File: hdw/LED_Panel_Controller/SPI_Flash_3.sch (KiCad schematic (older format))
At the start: 14 parts

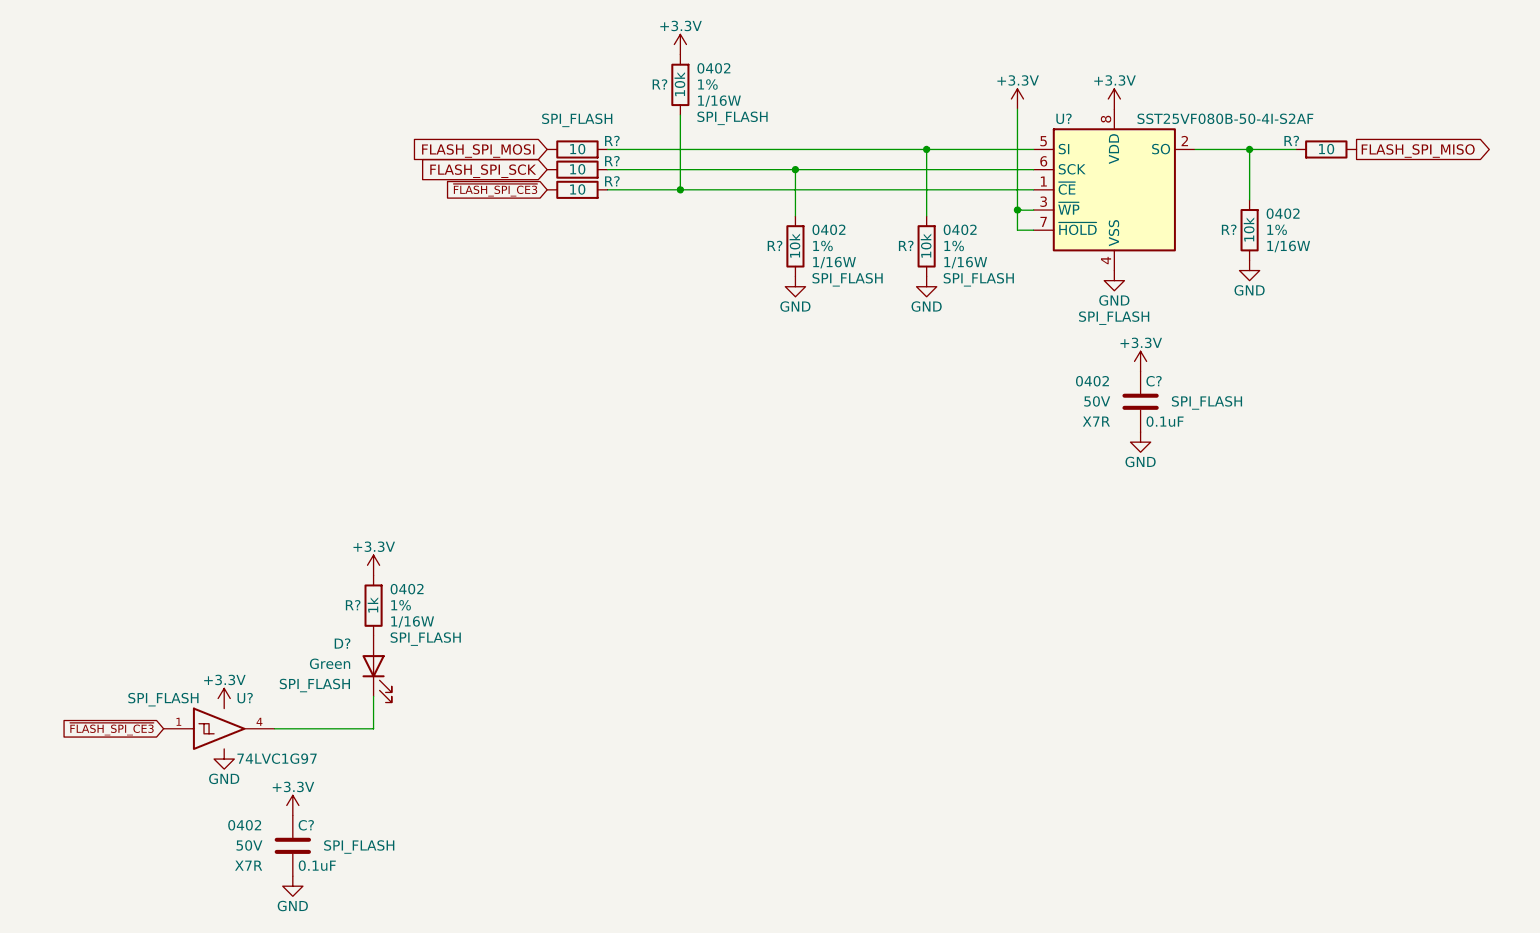
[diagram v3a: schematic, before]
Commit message: assigned I2C addresses
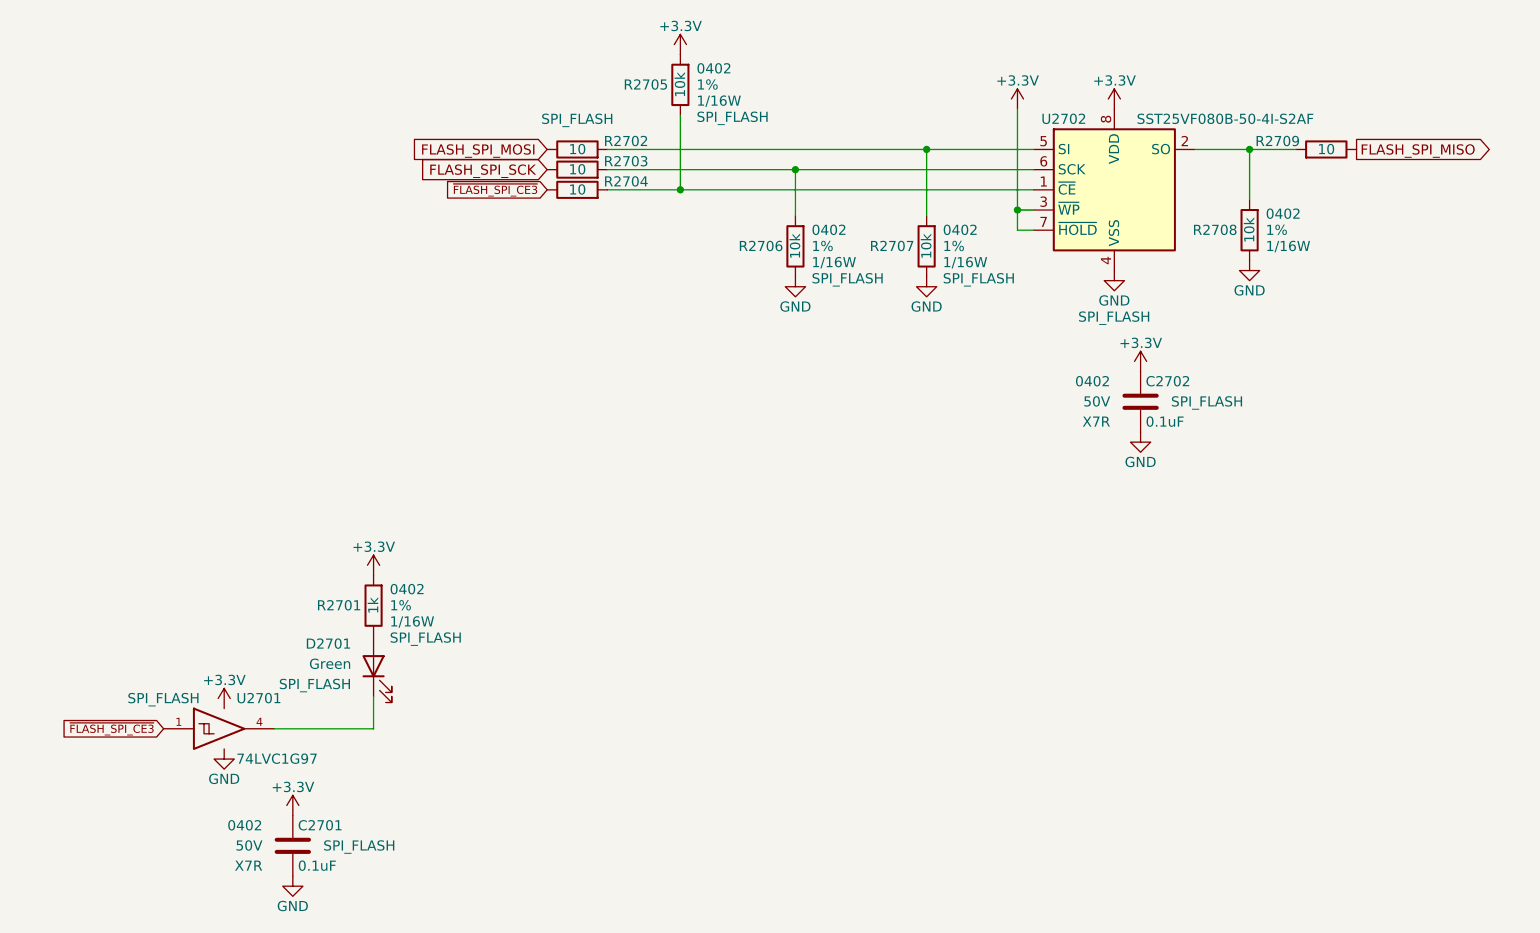
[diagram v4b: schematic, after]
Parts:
- removed C? (x2): 0.1uF, Capacitors_SMD:C_0402, symbol Custom_Library:C_Custom
- removed D?: Green, LEDs:LED_0402, symbol Device:LED
- removed R? (x3): 10k, Resistors_SMD:R_0402, symbol Custom_Library:R_Custom
- removed R? (x3): 10, Resistors_SMD:R_0402, symbol Custom_Library:R_Custom
- removed R?: 1k, Resistors_SMD:R_0402, symbol Custom_Library:R_Custom
- removed U?: SST25VF080B-50-4I-S2AF, Package_SO:SOIC-8_5.275x5.275mm_P1.27mm, symbol Memory_Flash:SST25VF080B-50-4x-S2Ax
- removed U?: 74LVC1G97, Package_TO_SOT_SMD:SOT-363_SC-70-6, symbol Custom_Library:74LVC1G97_Power_BUF
- added C2701, C2702: 0.1uF, Capacitors_SMD:C_0402, symbol Custom_Library:C_Custom
- added D2701: Green, LEDs:LED_0402, symbol Device:LED
- added R2701: 1k, Resistors_SMD:R_0402, symbol Custom_Library:R_Custom
- added R2702, R2703, R2704: 10, Resistors_SMD:R_0402, symbol Custom_Library:R_Custom
- added R2706, R2707, R2708: 10k, Resistors_SMD:R_0402, symbol Custom_Library:R_Custom
- added U2701: 74LVC1G97, Package_TO_SOT_SMD:SOT-363_SC-70-6, symbol Custom_Library:74LVC1G97_Power_BUF
- added U2702: SST25VF080B-50-4I-S2AF, Package_SO:SOIC-8_5.275x5.275mm_P1.27mm, symbol Memory_Flash:SST25VF080B-50-4x-S2Ax
- gave numbers to parts that had none: 2
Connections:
- net +3V3: now also C2701.1, C2702.1, R2701.1, U2701.5 (VCC), U2702.3 (~WP~), U2702.7 (~HOLD~), U2702.8 (VDD)
- net FLASH_SPI_MOSI: now also R2702.2
- net FLASH_SPI_SCK: now also R2703.2
- net GND: now also C2701.2, C2702.2, R2706.2, R2707.2, R2708.2, U2701.2 (GND), U2701.3 (GND), U2701.6 (GND), U2702.4 (VSS)
- net ~FLASH_SPI_CE3: now also R2704.2, U2701.1
- net at R2709.1: now also R2708.1, U2702.2 (SO)
- net at R2705.2: now also R2704.1, U2702.1 (~CE)
- new net: R2702.1, R2707.1, U2702.5 (SI)
- new net: D2701.1 (K), U2701.4
- new net: D2701.2 (A), R2701.2
- new net: R2703.1, R2706.1, U2702.6 (SCK)
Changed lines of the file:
@@
 $EndDescr
 $Comp
-L power:GND #PWR?
-U 1 1 5BB4E0E3
+L power:GND #PWR02711
+U 1 1 6078625E
 P 6080 4050
-F 0 "#PWR?" H 6080 3800 50  0001 C CNN
+F 0 "#PWR02711" H 6080 3800 50  0001 C CNN
 F 1 "GND" H 6080 3900 50  0000 C CNN
 F 2 "" H 6080 4050 50  0001 C CNN
@@
 $EndComp
 $Comp
-L Custom_Library:R_Custom R?
-U 1 1 5BB4EDD1
+L Custom_Library:R_Custom R2708
+U 1 1 60786267
 P 6750 3850
-F 0 "R?" H 6690 3850 50  0000 R CNN
+F 0 "R2708" H 6690 3850 50  0000 R CNN
 F 1 "10k" V 6750 3850 50  0000 C CNN
 F 2 "Resistors_SMD:R_0402" H 6750 3850 50  0001 C CNN
@@
 $EndComp
 $Comp
-L power:GND #PWR?
-U 1 1 5BB4EE63
+L power:GND #PWR02708
+U 1 1 60786270
 P 5150 4080
-F 0 "#PWR?" H 5150 3830 50  0001 C CNN
+F 0 "#PWR02708" H 5150 3830 50  0001 C CNN
 F 1 "GND" H 5150 3930 50  0000 C CNN
 F 2 "" H 5150 4080 50  0001 C CNN
@@
 $EndComp
 $Comp
-L power:GND #PWR?
-U 1 1 5BB4EE7C
+L power:GND #PWR02714
+U 1 1 60786275
 P 6750 4000
-F 0 "#PWR?" H 6750 3750 50  0001 C CNN
+F 0 "#PWR02714" H 6750 3750 50  0001 C CNN
 F 1 "GND" H 6750 3850 50  0000 C CNN
 F 2 "" H 6750 4000 50  0001 C CNN
@@
 $EndComp
 $Comp
-L Custom_Library:R_Custom R?
-U 1 1 5BB4F53B
+L Custom_Library:R_Custom R2702
+U 1 1 6078627E
 P 3420 3450
-F 0 "R?" V 3380 3580 50  0000 L CNN
+F 0 "R2702" V 3380 3580 50  0000 L CNN
 F 1 "10" V 3420 3450 50  0000 C CNN
 F 2 "Resistors_SMD:R_0402" H 3420 3450 50  0001 C CNN
@@
 	3570 3650 3930 3650
 $Comp
-L power:+3.3V #PWR?
-U 1 1 5BDF3D33
+L power:+3.3V #PWR02706
+U 1 1 60786281
 P 3930 2980
-F 0 "#PWR?" H 3930 2830 50  0001 C CNN
+F 0 "#PWR02706" H 3930 2830 50  0001 C CNN
 F 1 "+3.3V" H 3930 3120 50  0000 C CNN
 F 2 "" H 3930 2980 50  0001 C CNN
@@
 $EndComp
 $Comp
-L power:+3.3V #PWR?
-U 1 1 5BDF3DF4
+L power:+3.3V #PWR02710
+U 1 1 6078628A
 P 6080 3250
-F 0 "#PWR?" H 6080 3100 50  0001 C CNN
+F 0 "#PWR02710" H 6080 3100 50  0001 C CNN
 F 1 "+3.3V" H 6080 3390 50  0000 C CNN
 F 2 "" H 6080 3250 50  0001 C CNN
@@
 $Comp
 L Custom_Library:C_Custom C?
-U 1 1 5C15F697
+U 1 1 6078628E
 P 2010 6900
-AR Path="/5BAAE16C/5C15F697" Ref="C?"  Part="1"
-AR Path="/5BB181D8/5C15F697" Ref="C?"  Part="1"
-AR Path="/5BB2595E/5C15F697" Ref="C?"  Part="1"
-AR Path="/5F583577/5C15F697" Ref="C?"  Part="1"
-AR Path="/5F583598/5C15F697" Ref="C?"  Part="1"
-F 0 "C?" H 2035 7000 50  0000 L CNN
+AR Path="/5BAAE16C/6078628E" Ref="C?"  Part="1"
+AR Path="/5BB181D8/6078628E" Ref="C?"  Part="1"
+AR Path="/5BB2595E/6078628E" Ref="C?"  Part="1"
+AR Path="/5F583577/6078628E" Ref="C?"  Part="1"
+AR Path="/5F583598/6078628E" Ref="C2701"  Part="1"
+F 0 "C2701" H 2035 7000 50  0000 L CNN
 F 1 "0.1uF" H 2035 6800 50  0000 L CNN
 F 2 "Capacitors_SMD:C_0402" H 2048 6750 50  0001 C CNN
@@
 $EndComp
 $Comp
-L power:+3.3V #PWR?
-U 1 1 5C161B83
+L power:+3.3V #PWR02701
+U 1 1 6078629B
 P 1670 6220
-F 0 "#PWR?" H 1670 6070 50  0001 C CNN
+F 0 "#PWR02701" H 1670 6070 50  0001 C CNN
 F 1 "+3.3V" H 1670 6360 50  0000 C CNN
 F 2 "" H 1670 6220 50  0001 C CNN
@@
 $EndComp
 $Comp
-L power:+3.3V #PWR?
-U 1 1 5C161BE9
+L power:+3.3V #PWR02703
+U 1 1 6078629F
 P 2010 6750
-F 0 "#PWR?" H 2010 6600 50  0001 C CNN
+F 0 "#PWR02703" H 2010 6600 50  0001 C CNN
 F 1 "+3.3V" H 2010 6890 50  0000 C CNN
 F 2 "" H 2010 6750 50  0001 C CNN
@@
 $EndComp
 $Comp
-L power:GND #PWR?
-U 1 1 5C161C44
+L power:GND #PWR02704
+U 1 1 607862A4
 P 2010 7050
-F 0 "#PWR?" H 2010 6800 50  0001 C CNN
+F 0 "#PWR02704" H 2010 6800 50  0001 C CNN
 F 1 "GND" H 2010 6900 50  0000 C CNN
 F 2 "" H 2010 7050 50  0001 C CNN
@@
 $EndComp
 $Comp
-L power:GND #PWR?
-U 1 1 5C161C9F
+L power:GND #PWR02702
+U 1 1 607862AB
 P 1670 6420
-F 0 "#PWR?" H 1670 6170 50  0001 C CNN
+F 0 "#PWR02702" H 1670 6170 50  0001 C CNN
 F 1 "GND" H 1670 6270 50  0000 C CNN
 F 2 "" H 1670 6420 50  0001 C CNN
@@
 $Comp
 L power:+3.3V #PWR?
-U 1 1 5C166A81
+U 1 1 607862B2
 P 2410 5560
-AR Path="/5BB844FD/5C166A81" Ref="#PWR?"  Part="1"
-AR Path="/5BF346B3/5C166A81" Ref="#PWR?"  Part="1"
-AR Path="/5BB2595E/5C166A81" Ref="#PWR?"  Part="1"
-AR Path="/5F583577/5C166A81" Ref="#PWR?"  Part="1"
-AR Path="/5F583598/5C166A81" Ref="#PWR?"  Part="1"
-F 0 "#PWR?" H 2410 5410 50  0001 C CNN
+AR Path="/5BB844FD/607862B2" Ref="#PWR?"  Part="1"
+AR Path="/5BF346B3/607862B2" Ref="#PWR?"  Part="1"
+AR Path="/5BB2595E/607862B2" Ref="#PWR?"  Part="1"
+AR Path="/5F583577/607862B2" Ref="#PWR?"  Part="1"
+AR Path="/5F583598/607862B2" Ref="#PWR02705"  Part="1"
+F 0 "#PWR02705" H 2410 5410 50  0001 C CNN
 F 1 "+3.3V" H 2410 5700 50  0000 C CNN
 F 2 "" H 2410 5560 50  0001 C CNN
@@
 $Comp
 L Device:LED D?
-U 1 1 5C166A95
+U 1 1 607862BB
 P 2410 6010
-AR Path="/5BB844FD/5C166A95" Ref="D?"  Part="1"
-AR Path="/5BF346B3/5C166A95" Ref="D?"  Part="1"
-AR Path="/5BB2595E/5C166A95" Ref="D?"  Part="1"
-AR Path="/5F583577/5C166A95" Ref="D?"  Part="1"
-AR Path="/5F583598/5C166A95" Ref="D?"  Part="1"
-F 0 "D?" V 2520 6120 50  0000 L CNN
+AR Path="/5BB844FD/607862BB" Ref="D?"  Part="1"
+AR Path="/5BF346B3/607862BB" Ref="D?"  Part="1"
+AR Path="/5BB2595E/607862BB" Ref="D?"  Part="1"
+AR Path="/5F583577/607862BB" Ref="D?"  Part="1"
+AR Path="/5F583598/607862BB" Ref="D2701"  Part="1"
+F 0 "D2701" V 2520 6120 50  0000 L CNN
 F 1 "Green" V 2420 6120 50  0000 L CNN
 F 2 "LEDs:LED_0402" H 2410 6010 50  0001 C CNN
@@
 $EndComp
 $Comp
-L Memory_Flash:SST25VF080B-50-4x-S2Ax U?
-U 1 1 5F6879D5
+L Memory_Flash:SST25VF080B-50-4x-S2Ax U2702
+U 1 1 607862F9
 P 6080 3650
-F 0 "U?" H 5830 4000 50  0000 C CNN
+F 0 "U2702" H 5830 4000 50  0000 C CNN
 F 1 "SST25VF080B-50-4I-S2AF" H 6630 4000 50  0000 C CNN
 F 2 "Package_SO:SOIC-8_5.275x5.275mm_P1.27mm" H 6080 2950 50  0001 C CNN
@@
 $EndComp
 $Comp
-L power:+3.3V #PWR?
-U 1 1 5F689292
+L power:+3.3V #PWR02712
+U 1 1 60786301
 P 6210 4550
-F 0 "#PWR?" H 6210 4400 50  0001 C CNN
+F 0 "#PWR02712" H 6210 4400 50  0001 C CNN
 F 1 "+3.3V" H 6210 4690 50  0000 C CNN
 F 2 "" H 6210 4550 50  0001 C CNN
@@
 $EndComp
 $Comp
-L power:GND #PWR?
-U 1 1 5F689298
+L power:GND #PWR02713
+U 1 1 60786309
 P 6210 4850
-F 0 "#PWR?" H 6210 4600 50  0001 C CNN
+F 0 "#PWR02713" H 6210 4600 50  0001 C CNN
 F 1 "GND" H 6210 4700 50  0000 C CNN
 F 2 "" H 6210 4850 50  0001 C CNN
@@
 $EndComp
 $Comp
-L power:+3.3V #PWR?
-U 1 1 5F69329F
+L power:+3.3V #PWR02709
+U 1 1 60786310
 P 5600 3250
-F 0 "#PWR?" H 5600 3100 50  0001 C CNN
+F 0 "#PWR02709" H 5600 3100 50  0001 C CNN
 F 1 "+3.3V" H 5600 3390 50  0000 C CNN
 F 2 "" H 5600 3250 50  0001 C CNN
@@
 	3570 3550 4500 3550
 $Comp
-L Custom_Library:R_Custom R?
-U 1 1 5F697048
+L Custom_Library:R_Custom R2706
+U 1 1 60786312
 P 4500 3930
-F 0 "R?" H 4440 3930 50  0000 R CNN
+F 0 "R2706" H 4440 3930 50  0000 R CNN
 F 1 "10k" V 4500 3930 50  0000 C CNN
 F 2 "Resistors_SMD:R_0402" H 4500 3930 50  0001 C CNN
@@
 $EndComp
 $Comp
-L power:GND #PWR?
-U 1 1 5F697052
+L power:GND #PWR02707
+U 1 1 6078631E
 P 4500 4080
-F 0 "#PWR?" H 4500 3830 50  0001 C CNN
+F 0 "#PWR02707" H 4500 3830 50  0001 C CNN
 F 1 "GND" H 4500 3930 50  0000 C CNN
 F 2 "" H 4500 4080 50  0001 C CNN
@@
 	4500 3550 5680 3550
 $Comp
-L Custom_Library:R_Custom R?
-U 1 1 5F7379BB
+L Custom_Library:R_Custom R2703
+U 1 1 60786320
 P 3420 3550
-F 0 "R?" V 3380 3680 50  0000 L CNN
+F 0 "R2703" V 3380 3680 50  0000 L CNN
 F 1 "10" V 3420 3550 50  0000 C CNN
 F 2 "Resistors_SMD:R_0402" H 3420 3550 50  0001 C CNN
@@
 $EndComp
 $Comp
-L Custom_Library:R_Custom R?
-U 1 1 5F737B74
+L Custom_Library:R_Custom R2704
+U 1 1 6078632D
 P 3420 3650
-F 0 "R?" V 3380 3780 50  0000 L CNN
+F 0 "R2704" V 3380 3780 50  0000 L CNN
 F 1 "10" V 3420 3650 50  0000 C CNN
 F 2 "Resistors_SMD:R_0402" H 3420 3650 50  0001 C CNN
@@
 $EndComp
 $Comp
-L Custom_Library:R_Custom R?
+L Custom_Library:R_Custom R2709
 U 1 1 5F737D15
 P 7130 3450
-F 0 "R?" V 7090 3580 50  0000 L CNN
+F 0 "R2709" V 7090 3580 50  0000 L CNN
 F 1 "10" V 7130 3450 50  0000 C CNN
 F 2 "Resistors_SMD:R_0402" H 7130 3450 50  0001 C CNN
@@
 $EndComp
 $Comp
-L Custom_Library:74LVC1G97_Power_BUF U?
-U 1 1 5FE9D8D5
+L Custom_Library:74LVC1G97_Power_BUF U2701
+U 1 1 60786344
 P 1670 6320
-F 0 "U?" H 1730 6470 50  0000 L CNN
+F 0 "U2701" H 1730 6470 50  0000 L CNN
 F 1 "74LVC1G97" H 1730 6170 50  0000 L CNN
 F 2 "Package_TO_SOT_SMD:SOT-363_SC-70-6" H 1720 6320 50  0001 C CNN
@@
 $EndComp
 $Comp
-L Custom_Library:R_Custom R?
-U 1 1 6026393A
+L Custom_Library:R_Custom R2707
+U 1 1 60786359
 P 5150 3930
-F 0 "R?" H 5090 3930 50  0000 R CNN
+F 0 "R2707" H 5090 3930 50  0000 R CNN
 F 1 "10k" V 5150 3930 50  0000 C CNN
 F 2 "Resistors_SMD:R_0402" H 5150 3930 50  0001 C CNN
@@
 $EndComp
 $Comp
-L Custom_Library:R_Custom R?
+L Custom_Library:R_Custom R2705
 U 1 1 60263FB7
 P 3930 3130
-F 0 "R?" H 3870 3130 50  0000 R CNN
+F 0 "R2705" H 3870 3130 50  0000 R CNN
 F 1 "10k" V 3930 3130 50  0000 C CNN
 F 2 "Resistors_SMD:R_0402" H 3930 3130 50  0001 C CNN
@@
 $EndComp
 $Comp
-L Custom_Library:R_Custom R?
-U 1 1 60266213
+L Custom_Library:R_Custom R2701
+U 1 1 60786369
 P 2410 5710
-F 0 "R?" H 2350 5710 50  0000 R CNN
+F 0 "R2701" H 2350 5710 50  0000 R CNN
 F 1 "1k" V 2410 5710 50  0000 C CNN
 F 2 "Resistors_SMD:R_0402" H 2410 5710 50  0001 C CNN
@@
 $Comp
 L Custom_Library:C_Custom C?
-U 1 1 60269564
+U 1 1 6078636A
 P 6210 4700
-AR Path="/5BAAE16C/60269564" Ref="C?"  Part="1"
-AR Path="/5BB181D8/60269564" Ref="C?"  Part="1"
-AR Path="/5BB2595E/60269564" Ref="C?"  Part="1"
-AR Path="/5F583577/60269564" Ref="C?"  Part="1"
-AR Path="/5F583598/60269564" Ref="C?"  Part="1"
-F 0 "C?" H 6235 4800 50  0000 L CNN
+AR Path="/5BAAE16C/6078636A" Ref="C?"  Part="1"
+AR Path="/5BB181D8/6078636A" Ref="C?"  Part="1"
+AR Path="/5BB2595E/6078636A" Ref="C?"  Part="1"
+AR Path="/5F583577/6078636A" Ref="C?"  Part="1"
+AR Path="/5F583598/6078636A" Ref="C2702"  Part="1"
+F 0 "C2702" H 6235 4800 50  0000 L CNN
 F 1 "0.1uF" H 6235 4600 50  0000 L CNN
 F 2 "Capacitors_SMD:C_0402" H 6248 4550 50  0001 C CNN
